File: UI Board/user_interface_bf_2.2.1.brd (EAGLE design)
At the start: 119.3 x 74.8 mm, 20 parts, among them T1 2N3904, U1 PIC24FXXKA301_SPDIP, U2 MAX488, U3 CAT5, U4 7805TV, U6 3_PIN_FEMALE_HEADER, U7 3_PIN_FEMALE_HEADER, X2 F/CM12P

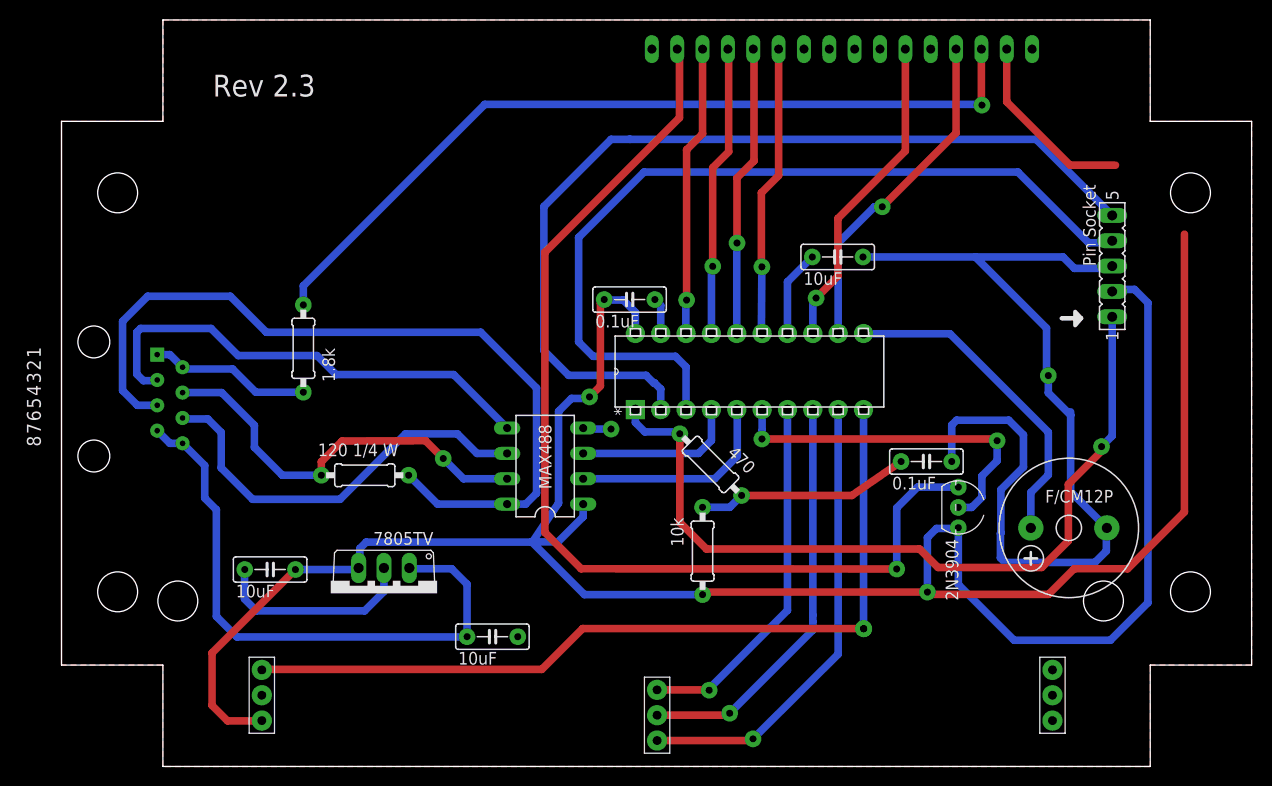
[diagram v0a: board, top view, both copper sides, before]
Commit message: 2.3.1
Updated version number
Updated Screw Positions
Fixed Missing Trace
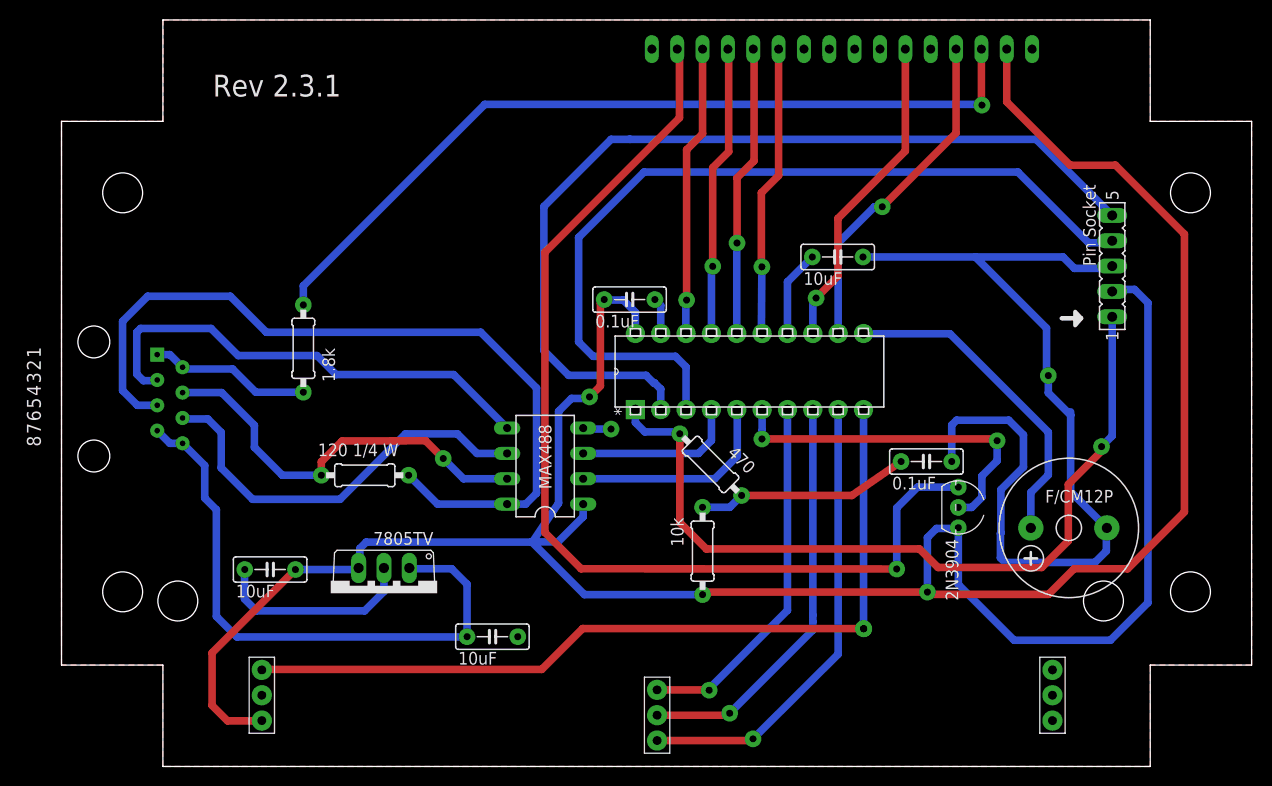
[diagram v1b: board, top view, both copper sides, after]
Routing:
- net +5V: track 280.0 -> 289.8 mm
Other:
- board text added: "Rev 2.3.1"
- board text removed: "Rev 2.3"
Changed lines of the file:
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@@
 <setting verticaltext="up"/>
 </settings>
-<grid distance="1" unitdist="mil" unit="mm" style="lines" multiple="1" display="yes" altdistance="0.025" altunitdist="inch" altunit="mm"/>
+<grid distance="1" unitdist="mil" unit="mil" style="lines" multiple="1" display="yes" altdistance="0.025" altunitdist="inch" altunit="mm"/>
 <layers>
 <layer number="1" name="Top" color="4" fill="1" visible="yes" active="yes"/>
@@
 <wire x1="109.093" y1="10.16" x2="109.093" y2="0" width="0" layer="20"/>
 <wire x1="109.093" y1="0" x2="10.16" y2="0" width="0" layer="20"/>
-<hole x="5.6261" y="17.5006" drill="4"/>
-<hole x="5.6261" y="57.4802" drill="4"/>
+<hole x="6.1269" y="17.5006" drill="4"/>
+<hole x="6.1269" y="57.4802" drill="4"/>
 <hole x="113.1269" y="57.4802" drill="4"/>
 <hole x="113.1269" y="17.5006" drill="4"/>
-<text x="15.1638" y="67.1322" size="2.1844" layer="21">Rev 2.3</text>
+<text x="15.1638" y="67.1322" size="2.1844" layer="21">Rev 2.3.1</text>
 <polygon width="0.4064" layer="21">
 <vertex x="100.203" y="44.9072"/>
@@
 <wire x1="101.473" y1="19.812" x2="106.8324" y2="19.812" width="0.762" layer="1"/>
 <wire x1="106.8324" y1="19.812" x2="112.522" y2="25.5016" width="0.762" layer="1"/>
+<wire x1="105.6132" y1="60.2488" x2="112.522" y2="53.34" width="0.762" layer="1"/>
 </signal>
 <signal name="A">
